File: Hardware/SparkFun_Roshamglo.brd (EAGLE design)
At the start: 33 x 72.4 mm, 37 parts, among them IC1 ATTINY84A, J1 ICSP, J2 USBPCB, Q1 500mA/300V, U1 IR-Receiver, U3 AP2112K-3.3V

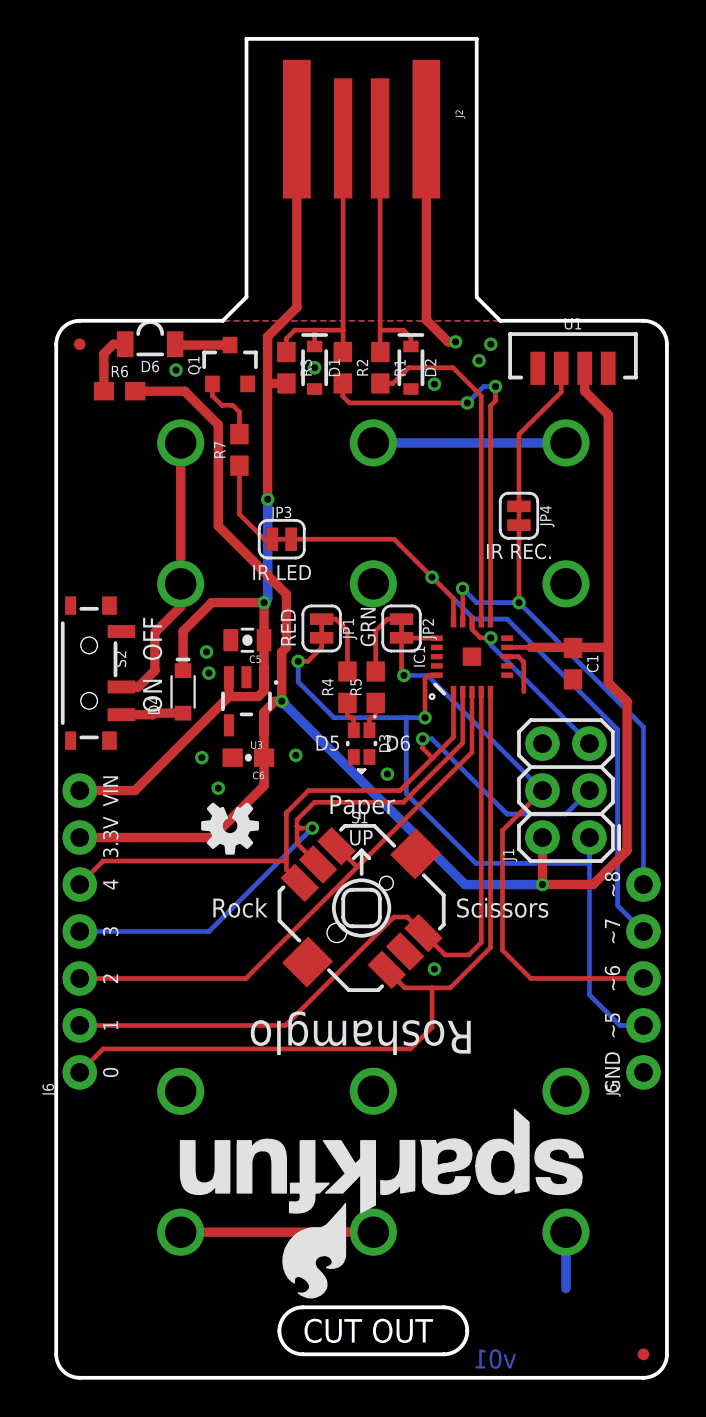
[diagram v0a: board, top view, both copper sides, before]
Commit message: Design Review Changes
- removed ISP
- added 10k to reset pin
- broke out reset pin
- Moved components away from SS pins
- Changed route out to dimmention layer
- moved lanyard hole away from edge of board
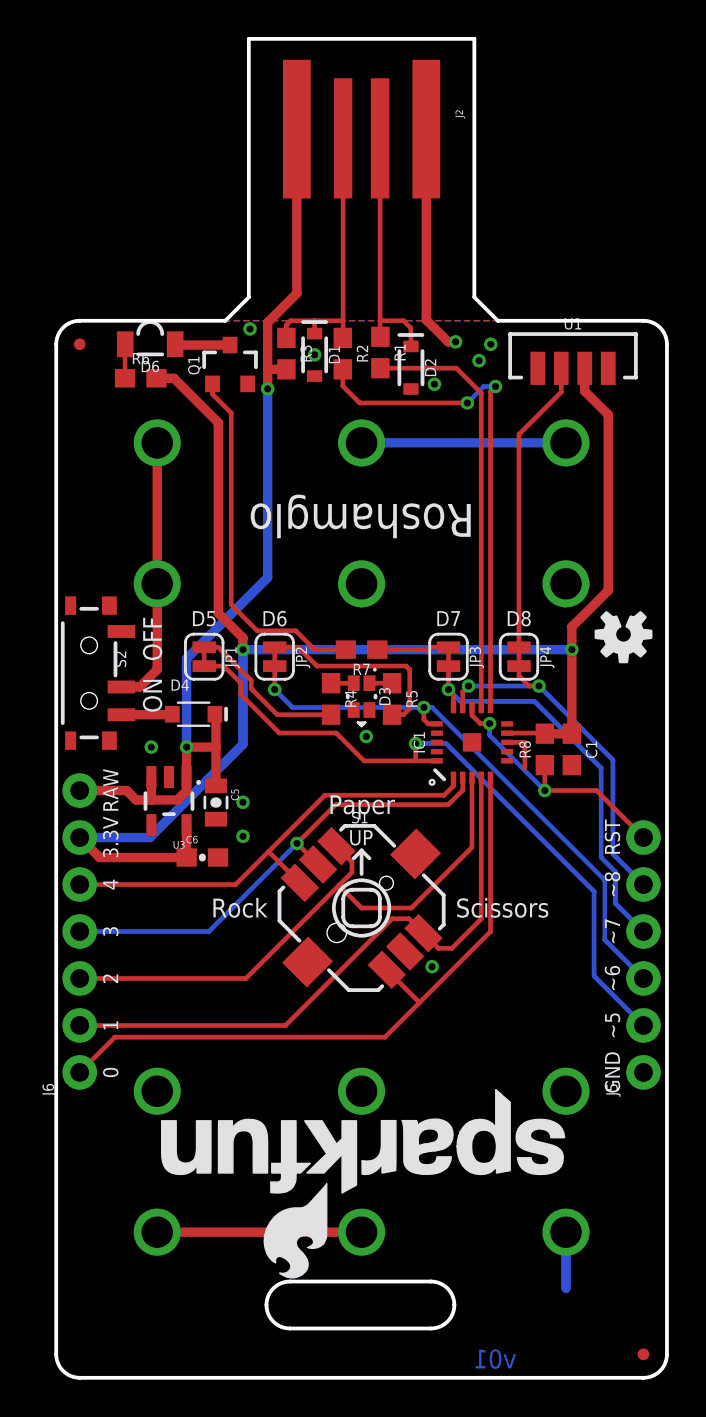
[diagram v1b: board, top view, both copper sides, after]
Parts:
- removed J1: ICSP, SparkFun-Connectors:2X3
- added R8: 10k, SparkFun-Resistors:0603
- J5: device SparkFun-Connectors:1X05_NO_SILK -> SparkFun-Connectors:1X06_NO_SILK
- moved LOGO1 23.7 mm to (30.7, 40.2)
- moved R7 12.7 mm to (16.5, 39.4), turned to 180 degrees
- moved JP3 11.0 mm to (21.2, 39.0), turned to 270 degrees
- moved C5 8.94 mm to (8.64, 31.1), turned to 270 degrees
- moved JP4 7.62 mm to (25.0, 39.0)
- moved JP2 7.03 mm to (11.8, 39.0)
- moved U3 6.83 mm to (6.10, 31.2)
- moved JP1 6.53 mm to (8.00, 39.0)
- moved C6 5.94 mm to (7.90, 28.1), turned to 0 degrees
- moved C1 4.64 mm to (27.9, 34.0)
- moved IC1 4.64 mm to (22.5, 34.4)
- moved D3 2.54 mm to (16.5, 36.8)
- moved LOGO2 1.48 mm to (28.2, 15.7)
- moved R6 1.34 mm to (4.57, 54.0)
- moved D4 1.34 mm to (7.43, 35.9), turned to 0 degrees
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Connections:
- net !RESET: now also J5.6, R8.1; no longer J1.5
- net 3.3V: now also R8.2; no longer J1.2
- net 4: no longer J1.3
- net 5: no longer J1.1
- net 6: no longer J1.4
- net GND: no longer J1.6
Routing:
- net 4: track 41.5 -> 25.3 mm, vias 1 -> 0
- net N$6: track 3.67 -> 19.6 mm
- net 7: track 36.3 -> 22.1 mm
- net 3.3V: track 96.7 -> 83.8 mm
- net N$9: track 8.41 -> 16.0 mm
- net 8: track 27.4 -> 20.0 mm
- net N$8: track 3.86 -> 11.0 mm
- net 0: track 42.9 -> 36.2 mm
- net 3: track 32.1 -> 26.2 mm
- net 1: track 38.8 -> 33.1 mm
- net 5: track 42.8 -> 37.3 mm, vias 2 -> 1
- net 10: track 22.3 -> 27.4 mm
- net N$7: track 3.86 -> 8.63 mm
- net !RESET: track 9.56 -> 14.2 mm, vias 1 -> 2
- net 9: track 18.6 -> 23.0 mm
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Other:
- outline, holes or cut-outs redrawn
- board text added: "D7"
- board text added: "D8"
- board text added: "RAW"
- board text added: "ROUTE OUT"
- board text added: "RST"
- board text removed: "CUT OUT"
- board text removed: "GRN"
- board text removed: "IR LED"
- board text removed: "IR REC."
- board text removed: "RED"
- board text removed: "VIN"

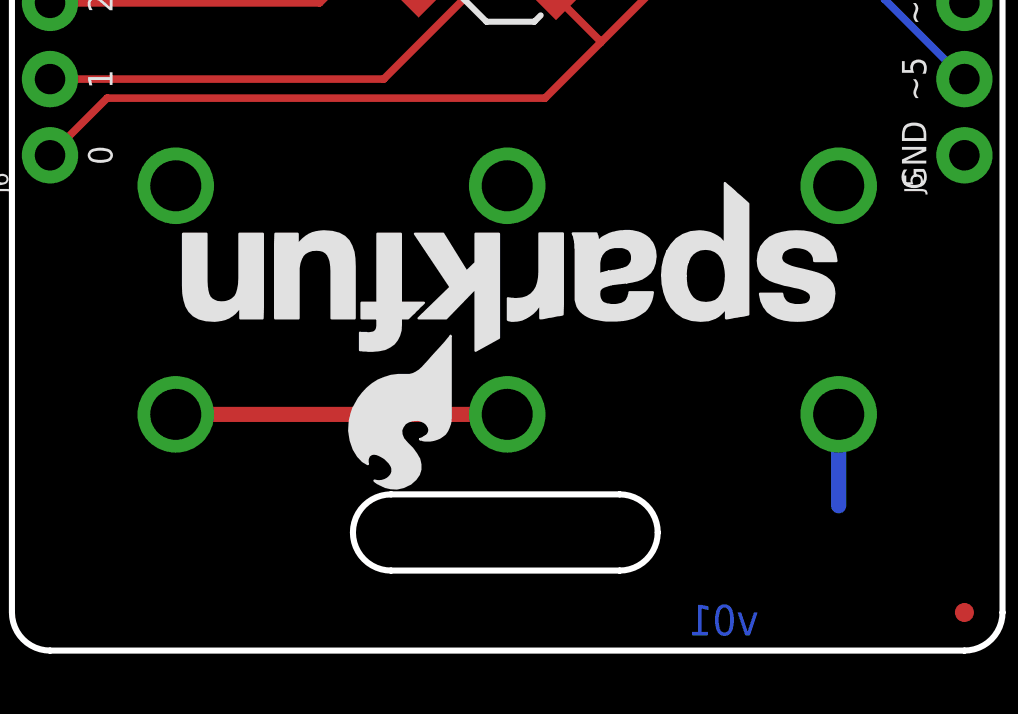
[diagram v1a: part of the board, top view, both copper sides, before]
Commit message: Fixed Battery t-stop and b-stop
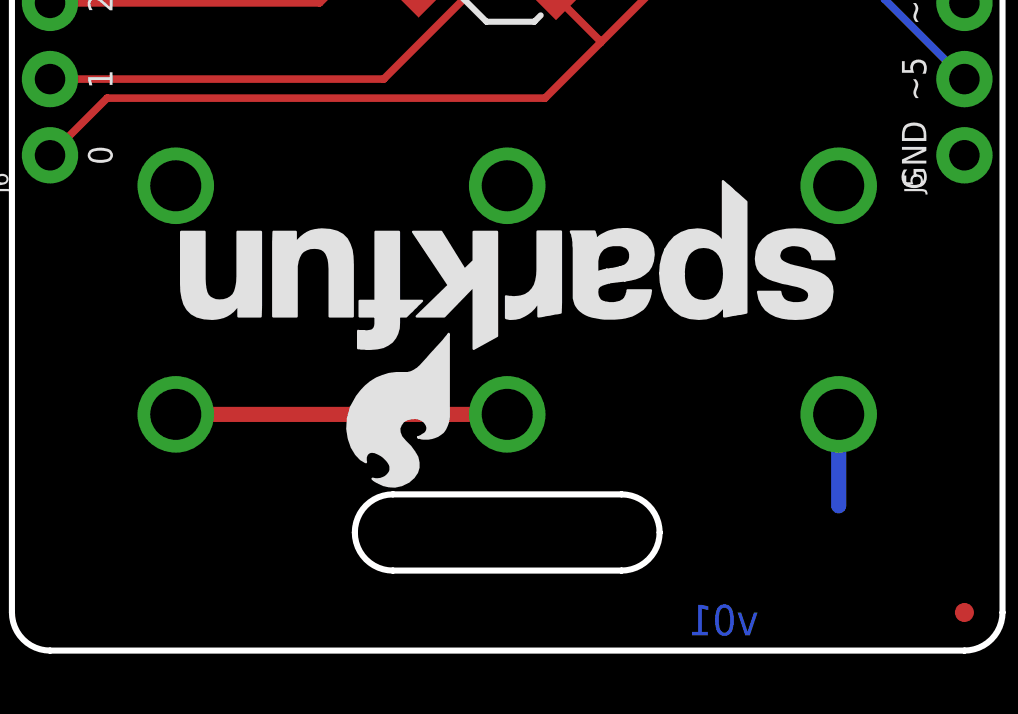
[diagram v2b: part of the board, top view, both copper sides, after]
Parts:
- moved LOGO2 0.09 mm to (28.1, 15.7)
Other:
- outline, holes or cut-outs redrawn
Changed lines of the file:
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@@
 <layer number="45" name="Holes" color="7" fill="1" visible="no" active="yes"/>
 <layer number="46" name="Milling" color="3" fill="1" visible="yes" active="yes"/>
-<layer number="47" name="Measures" color="7" fill="1" visible="no" active="yes"/>
+<layer number="47" name="Measures" color="7" fill="1" visible="yes" active="yes"/>
 <layer number="48" name="Document" color="7" fill="1" visible="no" active="yes"/>
 <layer number="49" name="Reference" color="7" fill="1" visible="no" active="yes"/>
@@
 <dimension x1="1.27" y1="0" x2="1.27" y2="57.15" x3="-5.08" y3="28.575" textsize="1.016" textratio="15" layer="47" unit="inch"/>
 <dimension x1="0" y1="1.27" x2="33.02" y2="1.27" x3="16.51" y3="-5.08" textsize="1.016" textratio="15" layer="47" unit="inch"/>
-<dimension x1="10.287" y1="57.15" x2="10.287" y2="67.31" x3="7.62" y3="62.23" textsize="1.016" textratio="15" layer="47" unit="inch"/>
-<dimension x1="10.287" y1="67.31" x2="22.733" y2="67.31" x3="16.51" y3="72.39" textsize="1.016" textratio="15" layer="47" unit="inch"/>
+<dimension x1="10.287" y1="57.15" x2="10.287" y2="72.3265" x3="7.62" y3="64.73825" textsize="1.016" textratio="15" layer="47" unit="inch"/>
+<dimension x1="10.414" y1="72.3265" x2="22.606" y2="72.3265" x3="16.51" y3="77.4065" textsize="1.016" textratio="15" layer="47" unit="inch"/>
 <dimension x1="31.75" y1="55.88" x2="32.648025" y2="56.778025" x3="38.16345625" y3="62.293459375" textsize="1.016" textratio="15" layer="47" dtype="radius" unit="inch"/>
 <dimension x1="31.75" y1="1.27" x2="32.885921875" y2="0.7020375" x3="39.86245" y3="-2.786234375" textsize="1.016" textratio="15" layer="47" dtype="radius" unit="inch"/>
@@
 <text x="25.019" y="40.64" size="0.8128" layer="21" font="vector" ratio="15" align="bottom-center">D8</text>
 <text x="30.48" y="29.21" size="0.8128" layer="21" font="vector" ratio="15" rot="R90" align="bottom-center">RST</text>
-<wire x1="12.6365" y1="5.207" x2="20.2565" y2="5.207" width="0.2032" layer="20"/>
-<wire x1="20.2565" y1="5.207" x2="21.5265" y2="3.937" width="0.2032" layer="20" curve="-90"/>
-<wire x1="21.5265" y1="3.937" x2="20.2565" y2="2.667" width="0.2032" layer="20" curve="-90"/>
-<wire x1="20.2565" y1="2.667" x2="12.6365" y2="2.667" width="0.2032" layer="20"/>
-<wire x1="12.6365" y1="2.667" x2="11.3665" y2="3.937" width="0.2032" layer="20" curve="-90"/>
-<wire x1="11.3665" y1="3.937" x2="12.6365" y2="5.207" width="0.2032" layer="20" curve="-90"/>
-<text x="16.51" y="3.4925" size="0.8128" layer="51" font="vector" ratio="15" align="bottom-center">ROUTE OUT</text>
+<wire x1="12.7" y1="5.207" x2="20.32" y2="5.207" width="0.2032" layer="20"/>
+<wire x1="20.32" y1="5.207" x2="21.59" y2="3.937" width="0.2032" layer="20" curve="-90"/>
+<wire x1="21.59" y1="3.937" x2="20.32" y2="2.667" width="0.2032" layer="20" curve="-90"/>
+<wire x1="20.32" y1="2.667" x2="12.7" y2="2.667" width="0.2032" layer="20"/>
+<wire x1="12.7" y1="2.667" x2="11.43" y2="3.937" width="0.2032" layer="20" curve="-90"/>
+<wire x1="11.43" y1="3.937" x2="12.7" y2="5.207" width="0.2032" layer="20" curve="-90"/>
+<text x="16.5735" y="3.4925" size="0.8128" layer="51" font="vector" ratio="15" align="bottom-center">ROUTE OUT</text>
 </plain>
 <attributes>
@@
 <element name="FD2" library="SparkFun-Aesthetics" package="FIDUCIAL-MICRO" value="FIDUCIALUFIDUCIAL" x="31.75" y="1.27"/>
 <element name="LOGO1" library="SparkFun-Aesthetics" package="OSHW-LOGO-S" value="OSHW-LOGOS" x="30.6705" y="40.1955" rot="R180"/>
-<element name="LOGO2" library="SparkFun-Aesthetics" package="SFE_LOGO_NAME_FLAME_.2" value="SFE_LOGO_NAME_FLAME.2_INCH" x="28.194" y="15.6845" rot="R180"/>
+<element name="LOGO2" library="SparkFun-Aesthetics" package="SFE_LOGO_NAME_FLAME_.2" value="SFE_LOGO_NAME_FLAME.2_INCH" x="28.1305" y="15.748" rot="R180"/>
 <element name="D6" library="Roshamglo" package="SFH4045N" value="LED-IR" x="5.08" y="55.88" rot="R180">
 <attribute name="PROD_ID" value="DIO-13574" x="5.08" y="55.88" size="1.778" layer="27" font="vector" ratio="15" rot="R180" display="off"/>

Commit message: Added logos
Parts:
- added H1, H2: STAND-OFF, SparkFun-Hardware:STAND-OFF
- added U$1: (no value), Roshamglo:ROSHAMGLO_PAPER
- added U$2: (no value), Roshamglo:ROSHAMGLO_ROCK
- added U$3: (no value), Roshamglo:ROSHAMGLO_SCISSORS
- added U$4: (no value), Roshamglo:ROSHAMGLO_LOGO_0.4
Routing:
- net GND: track 17.8 -> 19.8 mm
- net 5: track 37.3 -> 38.4 mm
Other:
- board text added: "@sparkfun"
- board text added: "Hack me! sfe.io/roshamglo"
- board text added: "Work hard. Play hardware."
- board text removed: "Paper"
- board text removed: "Rock"
- board text removed: "Scissors"
